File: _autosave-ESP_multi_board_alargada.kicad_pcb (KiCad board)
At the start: 2 copper layers, 24 parts, among them P101 CONN_01X02, P102 CONN_01X06, P103 CONN_01X02, P104 CONN_01X06, P105 CONN_01X12, P106 CONN_01X03, P107 CONN_I2C_MPU6050, P108 CONN_PINES_DIG, SW101 SW_PUSH_SMALL, SW102 SWITCH_INV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

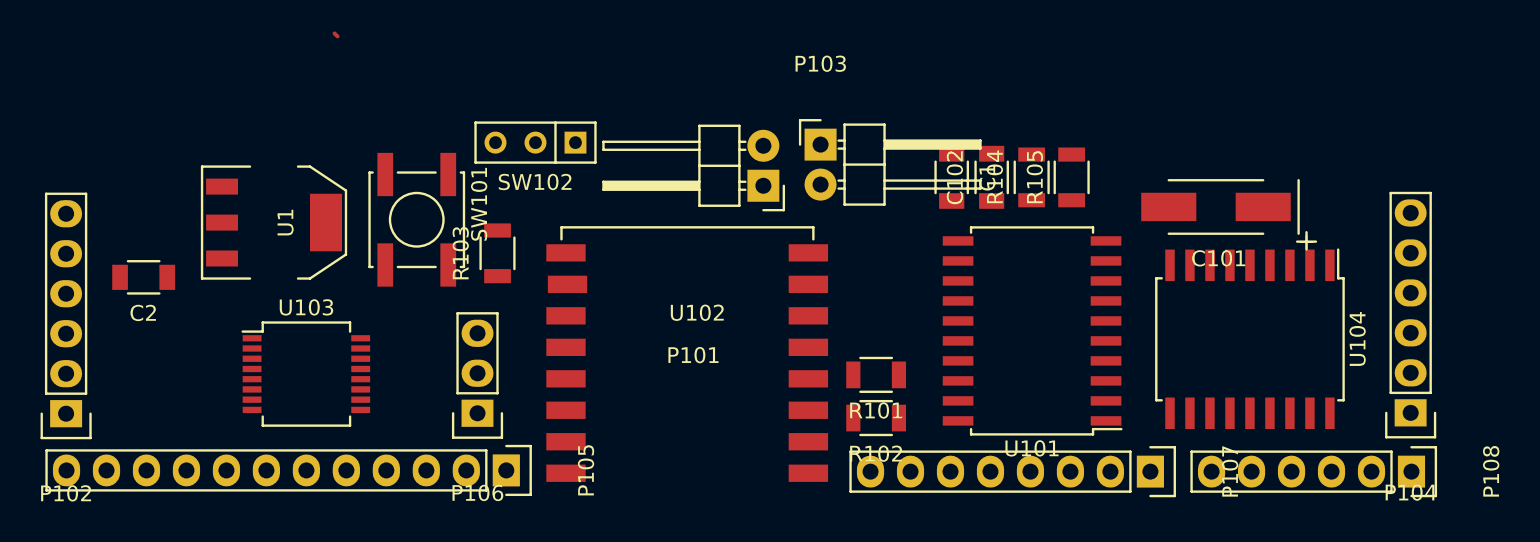
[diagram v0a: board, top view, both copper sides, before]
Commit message: cambios para hacer la version alargada mas compacta
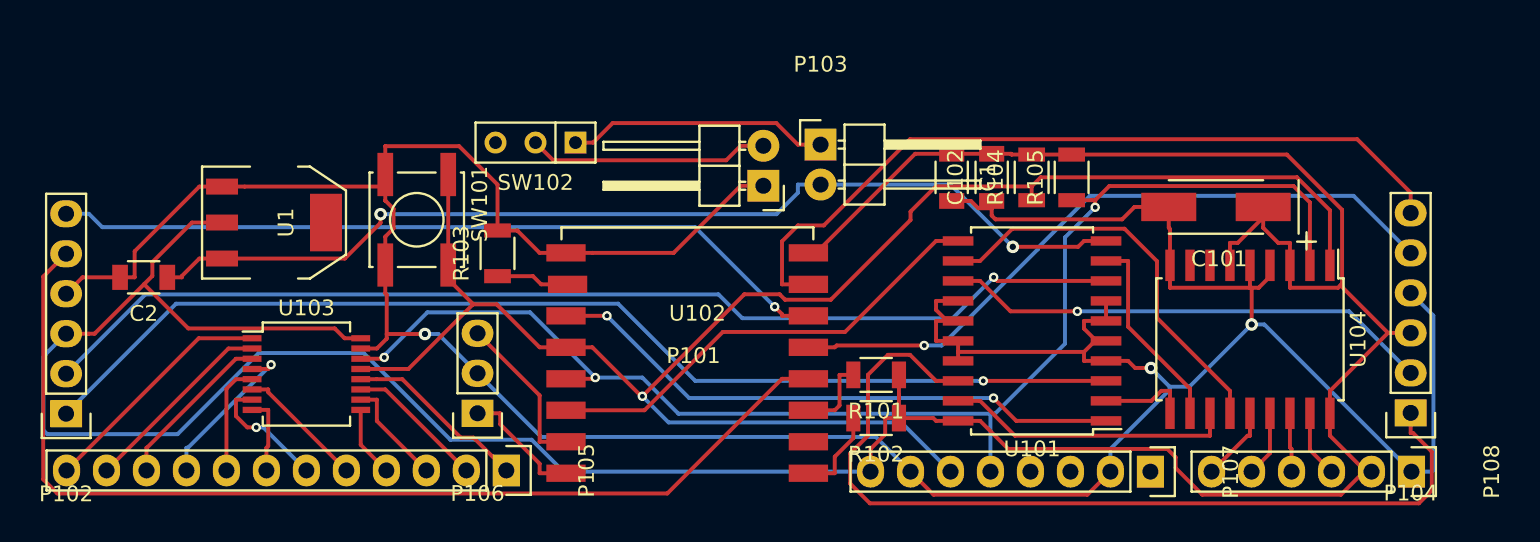
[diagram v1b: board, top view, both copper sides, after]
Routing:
- net GND: track 0.00 -> 221.7 mm, vias 0 -> 3
- net VDD: track 0.00 -> 207.9 mm
- net SCL: track 0.00 -> 107.8 mm, vias 0 -> 1
- net SDA: track 0.00 -> 85.3 mm, vias 0 -> 3
- net M1+: track 0.00 -> 71.0 mm, vias 0 -> 1
- net M1-: track 0.00 -> 70.0 mm, vias 0 -> 1
- net ENC1_A: track 0.00 -> 66.2 mm
- net VCC: track 0.00 -> 64.5 mm, vias 0 -> 2
- net M2+: track 0.00 -> 57.7 mm
- net ENC1_B: track 0.00 -> 49.2 mm, vias 0 -> 1
- net ENC2_B: track 0.00 -> 49.0 mm
- net ENC2_A: track 0.00 -> 44.5 mm, vias 0 -> 1
- net EN1: track 0.00 -> 36.4 mm, vias 0 -> 2
- net M2-: track 0.00 -> 31.2 mm, vias 0 -> 1
- net EN2: track 0.00 -> 28.7 mm
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
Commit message: routing
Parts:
- added D101: D, Diodes_ThroughHole:Diode_DO-35_SOD27_Horizontal_RM10, F.Cu at (167.1, 75.9)
- moved R104 0.10 mm to (188.9, 75.1)
- moved R105 0.10 mm to (191.4, 75.1)
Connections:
- P101 pad 2: Net-(P101-Pad2) -> Net-(D101-Pad1)
- SW102 pad 2: Net-(P101-Pad2) -> Net-(D101-Pad2)
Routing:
- net GND: track 221.7 -> 256.0 mm
- net M2+: track 57.7 -> 30.8 mm, vias 0 -> 1
- net ENC2_A: track 44.5 -> 67.4 mm, vias 1 -> 0
- net VCC: track 64.5 -> 80.6 mm, vias 2 -> 0
- net Net-(P101-Pad2): track 15.3 -> 0.00 mm
- net EN1: track 36.4 -> 45.5 mm, vias 2 -> 0
- net VDD: track 207.9 -> 199.3 mm
- net ENC2_B: track 49.0 -> 41.0 mm, vias 0 -> 1
- net Net-(D101-Pad1): track 0.00 -> 6.35 mm
- net Net-(D101-Pad2): track 0.00 -> 3.14 mm
- net SCL: track 107.8 -> 110.5 mm, vias 1 -> 4
- net M1-: track 70.0 -> 72.1 mm
- net EN2: track 28.7 -> 30.7 mm
- net M2_B: track 25.9 -> 24.0 mm, vias 0 -> 2
- net Net-(P105-Pad9): track 10.4 -> 8.67 mm, vias 1 -> 0
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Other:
- net class Default: trace_width 0.25 -> 0.3
- net class power: trace_width 0.25 -> 0.3
- net class small added: clearance 0.25, trace_width 0.25, via_dia 0.6, via_drill 0.4
- net class special added: clearance 0.2, trace_width 0.3, via_dia 0.6, via_drill 0.4
- net class special+ added: clearance 0.15, trace_width 0.3, via_dia 0.6, via_drill 0.4
